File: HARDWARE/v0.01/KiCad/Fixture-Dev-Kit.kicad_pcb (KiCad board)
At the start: 2 copper layers, 145.7 x 113.8 mm, 149 parts, among them J1 DUT, J10 SW_3, J11 FET_0, J12 FET_0, J13 NFET_0, J14 NFET_1, J15 Conn_01x20, J16 Conn_01x20, J17 CHIP4RH, J2 POWER, J20 Conn_01x20, J21 Conn_01x20, J23 CHIP4LH, J25 JST-2P-RA, J27 INA_40, J28 INA_40, J29 INA_40, J3 LED_0, J30 INA_40, J31 ADS, J4 LED_1, J5 LED_2, J6 LED_3, J7 SW_0, J8 SW_1, J9 SW_2, Q1 NTF2955T1G, Q10 NTF2955-D, Q11 NTF2955-D, Q12 NTF2955-D, Q13 FDN337N, Q14 FDN337N, Q15 FDN337N, Q16 FDN337N, Q2 NTF2955T1G, Q3 FDN337N, Q4 FDN337N, Q5 NTF2955-D, Q6 NTF2955-D, Q7 NTF2955-D, Q8 NTF2955-D, Q9 NTF2955-D, U1 INA219BIDCNT, U2 INA219BIDCNT, U3 INA219BIDCNT, U4 INA219BIDCNT, U5 ADS1015IDGST

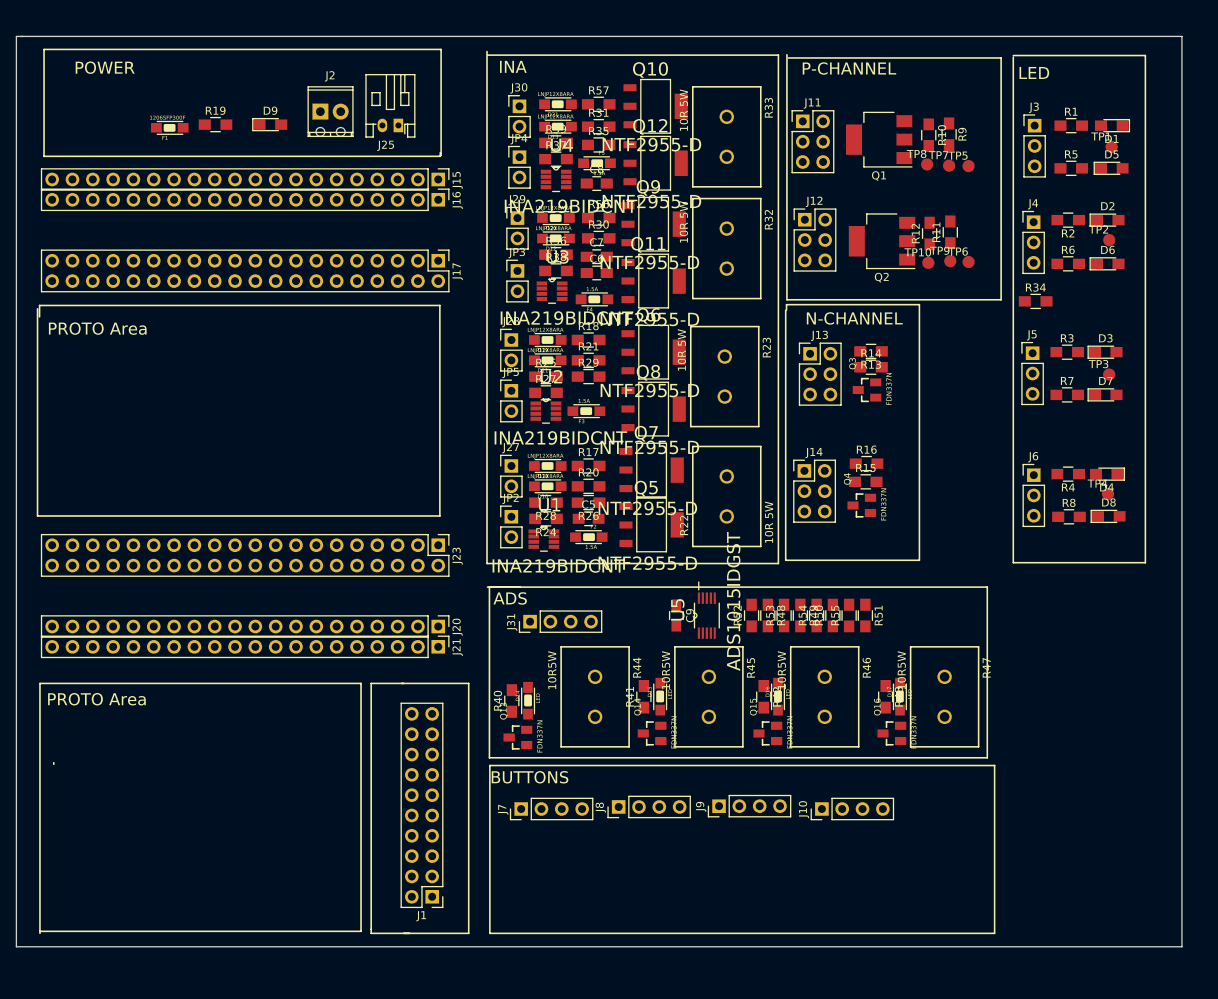
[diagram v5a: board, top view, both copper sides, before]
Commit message: updating layout footprints and board outline
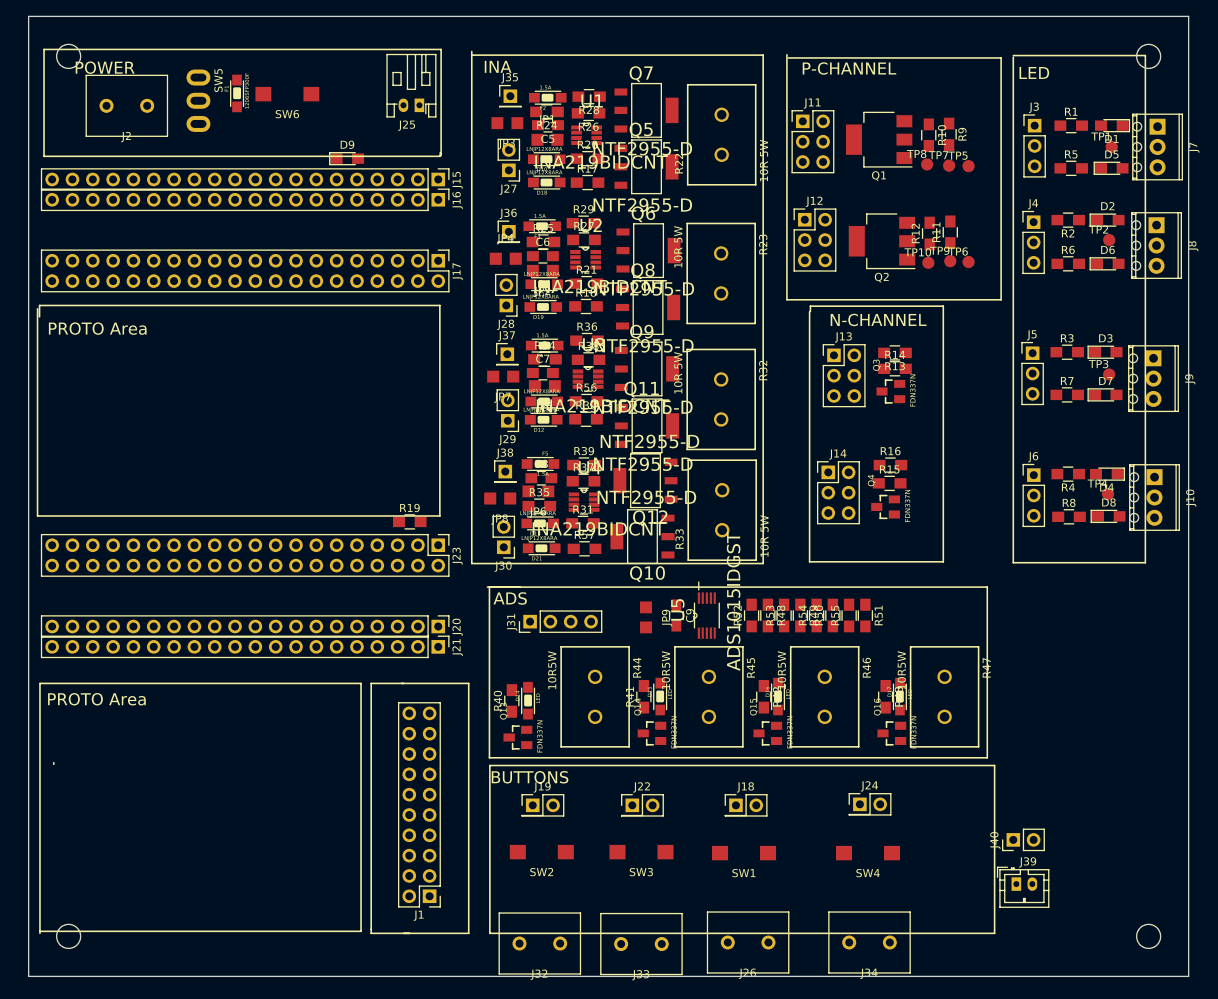
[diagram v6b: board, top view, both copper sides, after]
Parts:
- added J18: SW_0, Pin_Headers:Pin_Header_Straight_2x01_Pitch2.54mm, F.Cu at (113.4, 118.6)
- added J19: SW_0, Pin_Headers:Pin_Header_Straight_2x01_Pitch2.54mm, F.Cu at (88.0, 118.6)
- added J22: SW_0, Pin_Headers:Pin_Header_Straight_2x01_Pitch2.54mm, F.Cu at (100.5, 118.6)
- added J24: SW_0, Pin_Headers:Pin_Header_Straight_2x01_Pitch2.54mm, F.Cu at (128.9, 118.5)
- added J26: SW_0, TerminalBlocks:2Pin5.08, F.Cu at (114.9, 135.8)
- added J32: SW_0, TerminalBlocks:2Pin5.08, F.Cu at (88.9, 135.9)
- added J33: SW_0, TerminalBlocks:2Pin5.08, F.Cu at (101.6, 136.0)
- added J34: SW_0, TerminalBlocks:2Pin5.08, F.Cu at (130.1, 135.8)
- added J35: 40 V+, Pin_Headers:Pin_Header_Straight_1x01_Pitch2.54mm, F.Cu at (85.2, 30.0)
- added J36: 41 V+, Pin_Headers:Pin_Header_Straight_1x01_Pitch2.54mm, F.Cu at (85.0, 46.9)
- added J37: 42 V+, Pin_Headers:Pin_Header_Straight_1x01_Pitch2.54mm, F.Cu at (84.8, 62.2)
- added J38: 43 V+, Pin_Headers:Pin_Header_Straight_1x01_Pitch2.54mm, F.Cu at (84.6, 76.9)
- added J39: DUT BAT, Connectors_JST:JST_PH_B2B-PH-K_02x2.00mm_Straight, F.Cu at (148.5, 128.5)
- added J40: DUT BAT, Pin_Headers:Pin_Header_Straight_1x02_Pitch2.54mm, F.Cu at (148.1, 122.9)
- added JP1: Jumper_NC_Small, ConnectedCutJumper:connectedCutJumper, F.Cu at (89.9, 35.4)
- added JP6: Jumper_NC_Small, ConnectedCutJumper:connectedCutJumper, F.Cu at (88.7, 79.4)
- added JP7: Jumper_NC_Small, ConnectedCutJumper:connectedCutJumper, F.Cu at (84.3, 65.0)
- added JP8: Jumper_NC_Small, ConnectedCutJumper:connectedCutJumper, F.Cu at (83.9, 80.3)
- added JP9: Jumper_NC_Small, ConnectedCutJumper:connectedCutJumper, F.Cu at (102.2, 95.1)
- added SW1: TL9210AF260Q, TL9210AF260Q:TL9210AF260Q, F.Cu at (114.4, 124.6)
- added SW2: TL9210AF260Q, TL9210AF260Q:TL9210AF260Q, F.Cu at (89.2, 124.5)
- added SW3: TL9210AF260Q, TL9210AF260Q:TL9210AF260Q, F.Cu at (101.6, 124.5)
- added SW4: TL9210AF260Q, TL9210AF260Q:TL9210AF260Q, F.Cu at (129.9, 124.6)
- added SW5: YSS-19-1202-N, YSS-19-1202-N:YSS-19-1202-N, F.Cu at (46.2, 30.5)
- added SW6: TL9210AF260Q, TL9210AF260Q:TL9210AF260Q, F.Cu at (57.3, 29.7)
- J10: value SW_3 -> LED_2; footprint Pin_Headers:Pin_Header_Straight_1x04_Pitch2.54mm -> TerminalBlocks_Phoenix:TerminalBlock_Phoenix_MPT-2.54mm_3pol
- J2: footprint TerminalBlocks_Phoenix:TerminalBlock_Phoenix_MPT-2.54mm_2pol -> TerminalBlocks:2Pin5.08
- J7: value SW_0 -> LED_0; footprint Pin_Headers:Pin_Header_Straight_1x04_Pitch2.54mm -> TerminalBlocks_Phoenix:TerminalBlock_Phoenix_MPT-2.54mm_3pol
- J8: value SW_1 -> LED_1; footprint Pin_Headers:Pin_Header_Straight_1x04_Pitch2.54mm -> TerminalBlocks_Phoenix:TerminalBlock_Phoenix_MPT-2.54mm_3pol
- J9: value SW_2 -> LED_2; footprint Pin_Headers:Pin_Header_Straight_1x04_Pitch2.54mm -> TerminalBlocks_Phoenix:TerminalBlock_Phoenix_MPT-2.54mm_3pol
- JP2, JP3, JP4, JP5: value Jumper_NO -> Jumper_NC_Small; footprint Pin_Headers:Pin_Header_Straight_1x02_Pitch2.54mm -> ConnectedCutJumper:connectedCutJumper
- R48, R49, R50, R51: value 1K -> NC
- R52: value 1K -> 0R
- R53, R54, R55: value 1K -> 1R
- moved J7 116.6 mm to (166.1, 33.8), turned to 270 degrees
- moved J8 99.0 mm to (166.0, 46.1), turned to 270 degrees
- moved J9 78.0 mm to (165.6, 62.7), turned to 270 degrees
- moved R34 61.8 mm to (89.5, 62.9)
- moved J10 58.7 mm to (165.7, 77.6), turned to 270 degrees
- moved R57 55.6 mm to (94.5, 86.6)
- moved D21 55.5 mm to (89.2, 86.5)
- moved R19 55.3 mm to (72.6, 83.2)
- moved F2 55.2 mm to (89.9, 30.2), turned to 0 degrees
- moved J30 55.2 mm to (84.4, 86.4), turned to 180 degrees
- moved Q10 53.8 mm to (101.7, 85.0), turned to 180 degrees
- moved R28 51.0 mm to (95.1, 30.0)
- moved R24 50.9 mm to (89.8, 31.9)
- moved U1 50.8 mm to (94.7, 34.9)
- moved D13 49.6 mm to (89.0, 83.4)
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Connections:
- C9 pad 1: +5V -> Net-(C9-Pad1)
- F1 pad 1: (no net) -> Net-(F1-Pad1)
- F2 pad 2: +5V -> Net-(F2-Pad2)
- F3 pad 2: +5V -> Net-(F3-Pad2)
- F4 pad 2: +5V -> Net-(F4-Pad2)
- F5 pad 2: +5V -> Net-(F5-Pad2)
- J10 pad 1: (no net) -> Net-(J10-Pad1)
- J10 pad 2: (no net) -> Net-(D4-Pad1)
- J10 pad 3: (no net) -> GND
- J6 pad 1: Net-(J6-Pad1) -> Net-(J10-Pad1)
- J7 pad 1: (no net) -> Net-(J3-Pad1)
- J7 pad 2: (no net) -> Net-(D1-Pad1)
- J7 pad 3: (no net) -> GND
- J8 pad 1: (no net) -> Net-(J4-Pad1)
- J8 pad 2: (no net) -> Net-(D2-Pad1)
- J8 pad 3: (no net) -> GND
- J9 pad 1: (no net) -> Net-(J5-Pad1)
- J9 pad 2: (no net) -> Net-(D3-Pad1)
- J9 pad 3: (no net) -> GND
- JP2 pad 2: Net-(C5-Pad2) -> Net-(C6-Pad2)
- JP3 pad 1: /C4-VCC-3V3 -> Net-(JP3-Pad1)
- JP3 pad 2: Net-(C6-Pad2) -> /INA40_V-
- JP4 pad 1: /C4-VCC-3V3 -> Net-(JP4-Pad1)
- JP4 pad 2: Net-(C7-Pad2) -> /INA41_V-
- JP5 pad 2: Net-(C8-Pad2) -> Net-(C7-Pad2)
- R24 pad 2: /INA40_V- -> Net-(JP3-Pad1)
- R25 pad 2: /INA41_V- -> Net-(JP4-Pad1)
- R34 pad 2: /INA42_V- -> Net-(JP7-Pad1)
- R35 pad 2: /INA43_V- -> Net-(JP8-Pad1)
- R4 pad 2: Net-(J6-Pad1) -> Net-(J10-Pad1)
- U1 pad 2: /INA40_V- -> Net-(JP3-Pad1)
- U2 pad 2: /INA41_V- -> Net-(JP4-Pad1)
- U3 pad 2: /INA42_V- -> Net-(JP7-Pad1)
- U4 pad 2: /INA43_V- -> Net-(JP8-Pad1)
- U5 pad 8: +5V -> Net-(C9-Pad1)
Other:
- board size 145.7 x 113.8 mm -> 145 x 120 mm

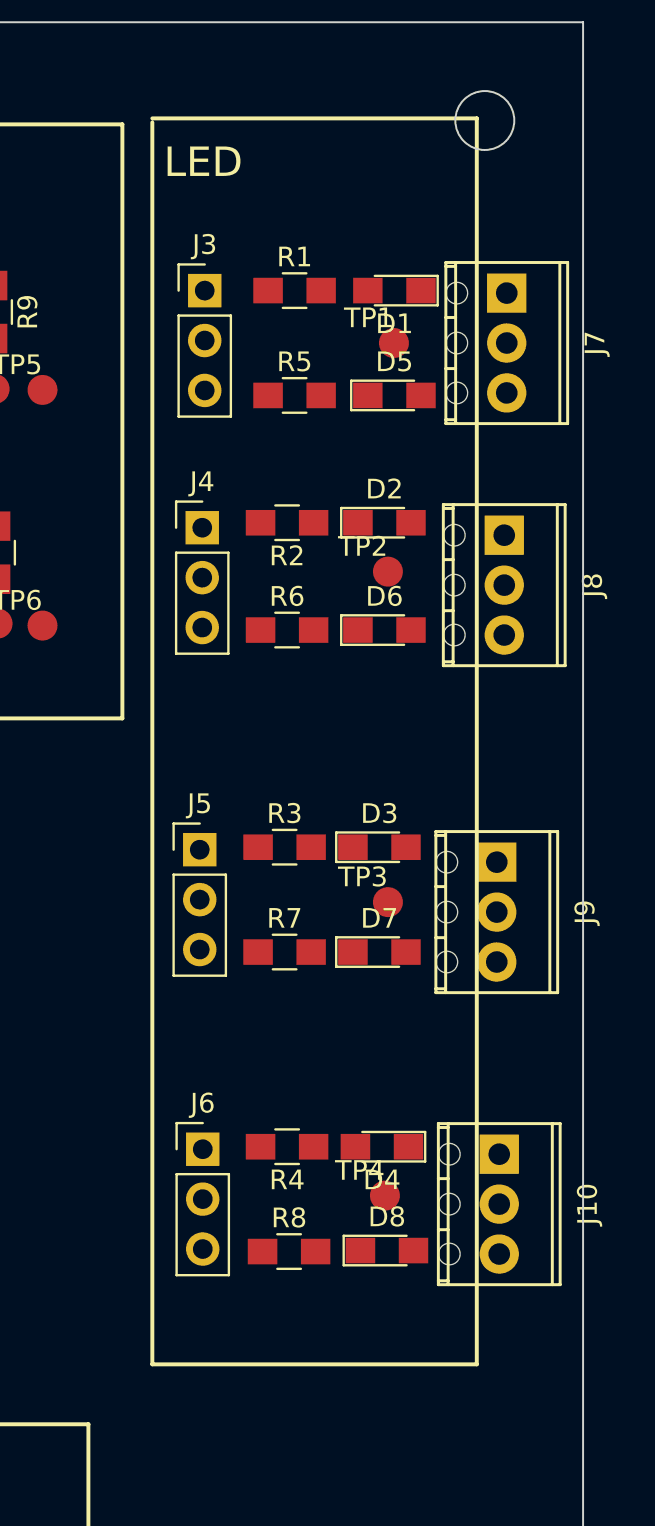
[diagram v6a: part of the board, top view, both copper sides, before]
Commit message: updaing LED screw terminal foot print
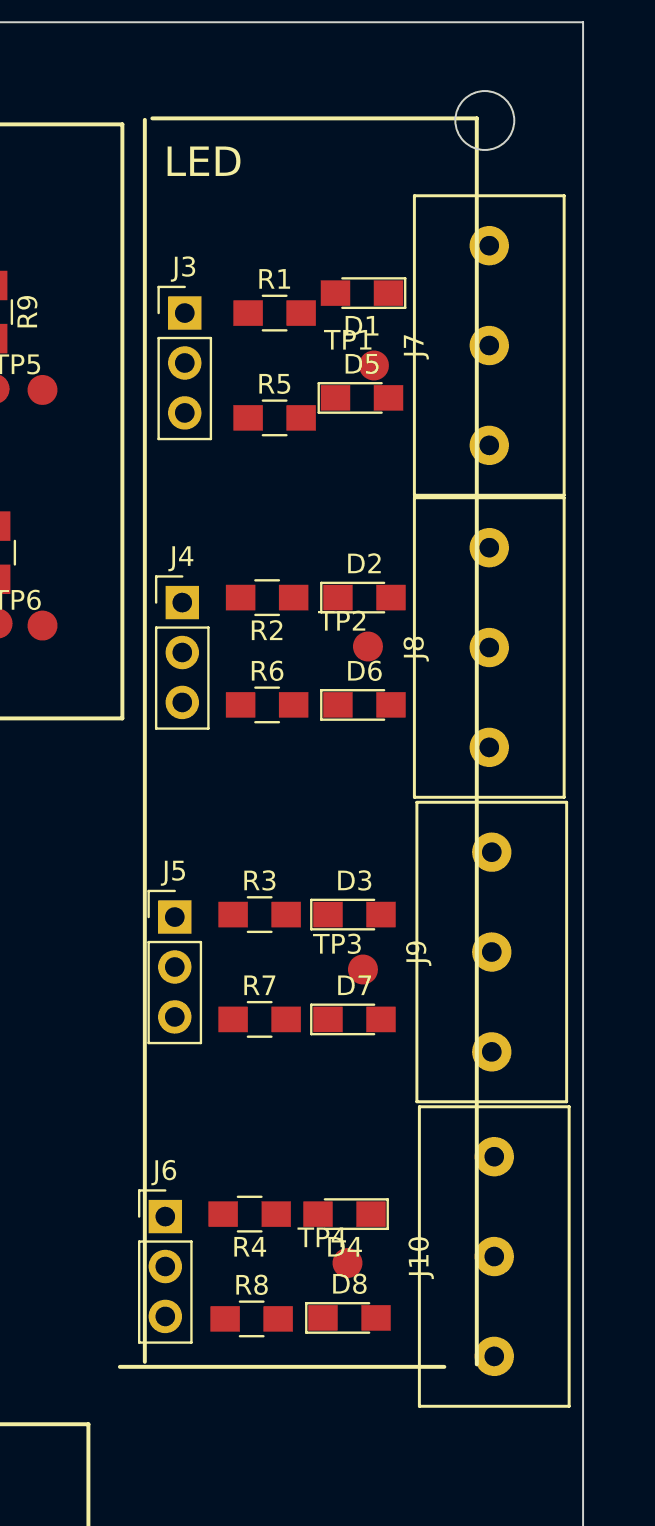
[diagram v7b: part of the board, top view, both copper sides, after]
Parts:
- J10: value LED_2 -> LED_3; footprint TerminalBlocks_Phoenix:TerminalBlock_Phoenix_MPT-2.54mm_3pol -> TerminalBlocks:3Pin5.08
- J7, J8, J9: footprint TerminalBlocks_Phoenix:TerminalBlock_Phoenix_MPT-2.54mm_3pol -> TerminalBlocks:3Pin5.08
- moved J8 5.77 mm to (165.2, 51.8)
- moved J10 5.21 mm to (165.5, 82.8)
- moved J9 4.58 mm to (165.4, 67.3)
- moved J4 3.94 mm to (149.6, 49.5)
- moved D2 3.94 mm to (158.9, 49.3)
- moved D6 3.94 mm to (158.9, 54.7)
- moved R2 3.94 mm to (153.9, 49.3)
- moved R6 3.94 mm to (153.9, 54.7)
- moved TP2 3.94 mm to (159.1, 51.8)
- moved D4 3.92 mm to (157.9, 80.6)
- moved D8 3.92 mm to (158.1, 85.9)
- moved J6 3.92 mm to (148.7, 80.8)
- moved R4 3.92 mm to (153.0, 80.6)
- moved R8 3.92 mm to (153.1, 86.0)
- moved TP4 3.92 mm to (158.0, 83.1)
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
